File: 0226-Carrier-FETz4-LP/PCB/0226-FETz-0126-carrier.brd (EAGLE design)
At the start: 27.9 x 21.6 mm, 3 parts

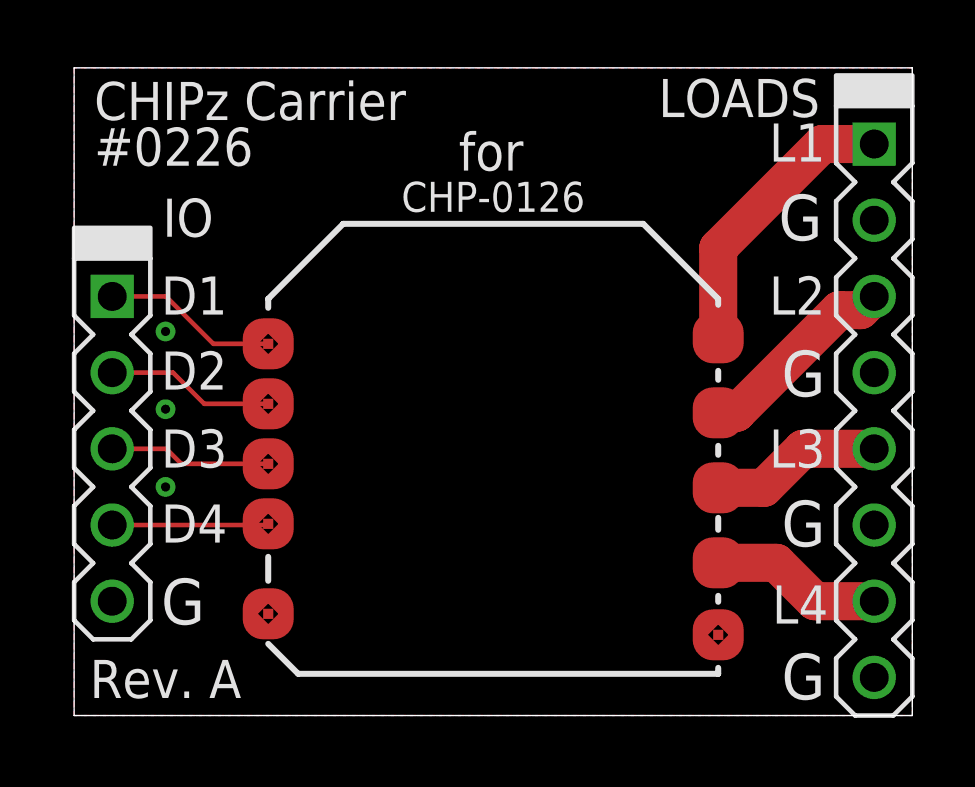
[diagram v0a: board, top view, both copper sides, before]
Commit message: Big batch of new PCBs sent to FAB.
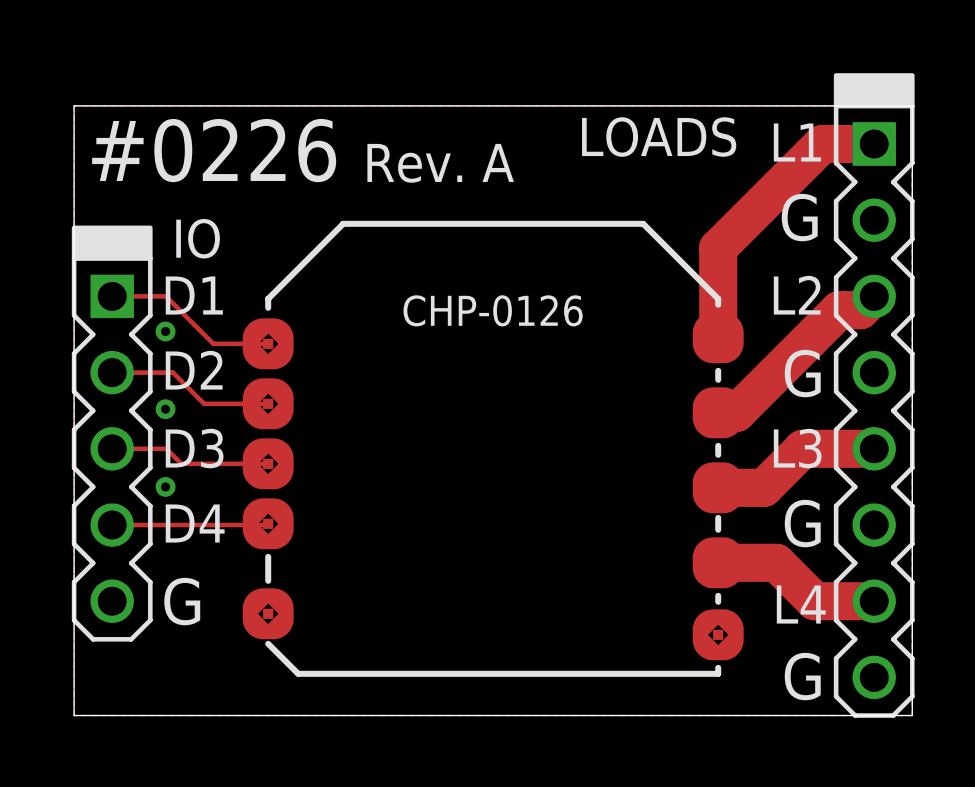
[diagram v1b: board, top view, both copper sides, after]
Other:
- board size 27.9 x 21.6 mm -> 27.9 x 20.3 mm
- board text added: "#0226"
- board text added: "CHIPz Carrier for #0126 Four Channel FET (High Power)"
- board text added: "Circuit Monkey"
- board text removed: "CHIPz Carrier #0226"
- board text removed: "by Circuit Monkey"
- board text removed: "for"
